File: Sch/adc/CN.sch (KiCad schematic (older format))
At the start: 19 parts, among them J1 JP4, J2 Header5, P1 CONN_02X40, U1 LTC2292

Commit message: Adding parts
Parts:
- C53: footprint (none) -> Capacitors_SMD:C_0603
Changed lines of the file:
@@
 F 0 "C53" H 3175 7050 50  0000 L CNN
 F 1 "0.1u" H 3175 6850 50  0000 L CNN
-F 2 "" H 3188 6800 50  0001 C CNN
+F 2 "Capacitors_SMD:C_0603" H 3188 6800 50  0001 C CNN
 F 3 "" H 3150 6950 50  0000 C CNN
 	1    3150 6950

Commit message: Add parts
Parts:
- J1: footprint (none) -> Pin_Headers:Pin_Header_Straight_2x04_Pitch2.54mm
- J2: footprint (none) -> Pin_Headers:Pin_Header_Straight_1x05_Pitch2.54mm
- R1, R12, R24, R25, R26: footprint (none) -> Resistors_SMD:R_0603
- R10, R11: value 49k -> 10k; footprint (none) -> Resistors_SMD:R_0603
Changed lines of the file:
@@
 F 0 "R24" V 1880 6150 50  0000 C CNN
 F 1 "1k" V 1800 6150 50  0000 C CNN
-F 2 "" V 1730 6150 50  0001 C CNN
+F 2 "Resistors_SMD:R_0603" V 1730 6150 50  0001 C CNN
 F 3 "" H 1800 6150 50  0000 C CNN
 	1    1800 6150
@@
 F 0 "R25" V 1880 6550 50  0000 C CNN
 F 1 "1k" V 1800 6550 50  0000 C CNN
-F 2 "" V 1730 6550 50  0001 C CNN
+F 2 "Resistors_SMD:R_0603" V 1730 6550 50  0001 C CNN
 F 3 "" H 1800 6550 50  0000 C CNN
 	1    1800 6550
@@
 F 0 "R26" V 1880 6950 50  0000 C CNN
 F 1 "1k" V 1800 6950 50  0000 C CNN
-F 2 "" V 1730 6950 50  0001 C CNN
+F 2 "Resistors_SMD:R_0603" V 1730 6950 50  0001 C CNN
 F 3 "" H 1800 6950 50  0000 C CNN
 	1    1800 6950
@@
 F 0 "J1" H 2600 6350 60  0000 C CNN
 F 1 "JP4" H 2600 7000 60  0000 C CNN
-F 2 "" H 2550 6900 60  0001 C CNN
+F 2 "Pin_Headers:Pin_Header_Straight_2x04_Pitch2.54mm" H 2550 6900 60  0001 C CNN
 F 3 "" H 2550 6900 60  0001 C CNN
 	1    2550 6650
@@
 F 0 "J2" H 8350 1850 60  0000 C CNN
 F 1 "Header5" H 8400 2500 60  0000 C CNN
-F 2 "" H 8350 2250 60  0001 C CNN
+F 2 "Pin_Headers:Pin_Header_Straight_1x05_Pitch2.54mm" H 8350 2250 60  0001 C CNN
 F 3 "" H 8350 2250 60  0001 C CNN
 	1    8350 2150
@@
 F 0 "R1" V 1030 2800 50  0000 C CNN
 F 1 "10k" V 950 2800 50  0000 C CNN
-F 2 "" V 880 2800 50  0001 C CNN
+F 2 "Resistors_SMD:R_0603" V 880 2800 50  0001 C CNN
 F 3 "" H 950 2800 50  0000 C CNN
 	1    950  2800
@@
 P 1600 3200
 F 0 "R10" V 1680 3200 50  0000 C CNN
-F 1 "49k" V 1600 3200 50  0000 C CNN
-F 2 "" V 1530 3200 50  0001 C CNN
+F 1 "10k" V 1600 3200 50  0000 C CNN
+F 2 "Resistors_SMD:R_0603" V 1530 3200 50  0001 C CNN
 F 3 "" H 1600 3200 50  0000 C CNN
 	1    1600 3200
@@
 P 1750 3200
 F 0 "R11" V 1830 3200 50  0000 C CNN
-F 1 "49k" V 1750 3200 50  0000 C CNN
-F 2 "" V 1680 3200 50  0001 C CNN
+F 1 "10k" V 1750 3200 50  0000 C CNN
+F 2 "Resistors_SMD:R_0603" V 1680 3200 50  0001 C CNN
 F 3 "" H 1750 3200 50  0000 C CNN
 	1    1750 3200
@@
 F 0 "R12" V 5880 4050 50  0000 C CNN
 F 1 "22" V 5800 4050 50  0000 C CNN
-F 2 "" V 5730 4050 50  0001 C CNN
+F 2 "Resistors_SMD:R_0603" V 5730 4050 50  0001 C CNN
 F 3 "" H 5800 4050 50  0000 C CNN
 	1    5800 4050

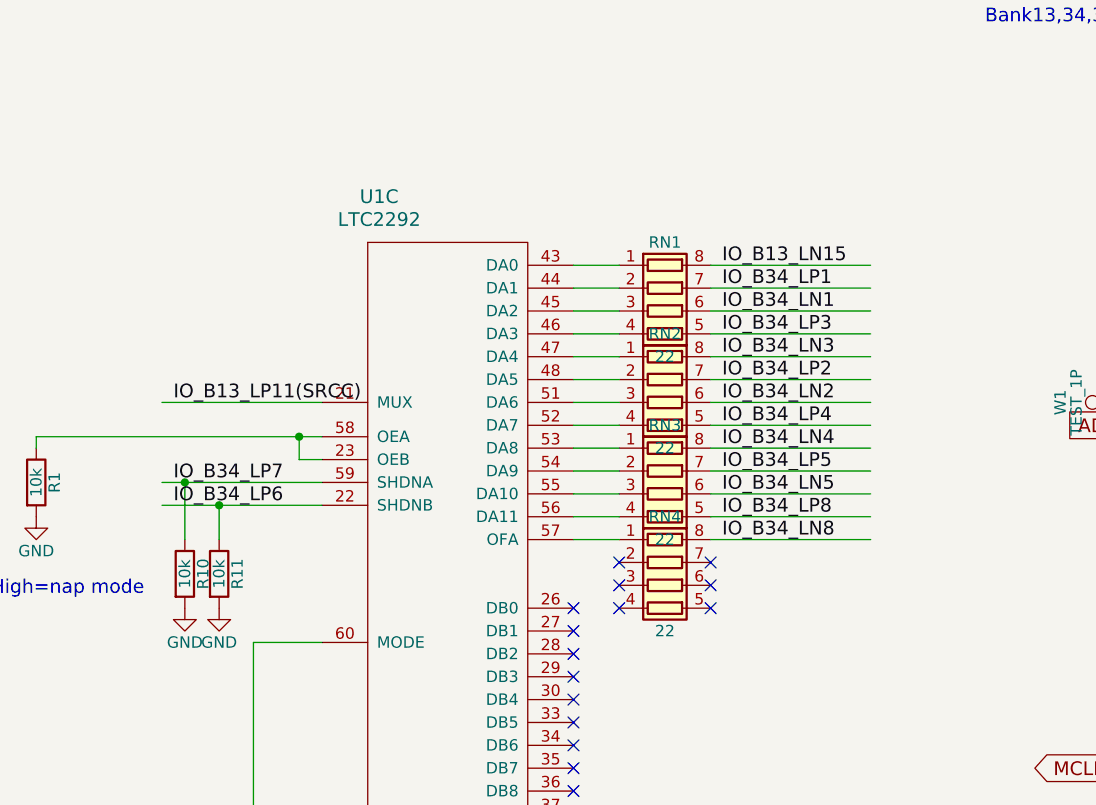
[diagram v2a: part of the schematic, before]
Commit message: Changed TCXO->MEMS TCXO. BOM finished
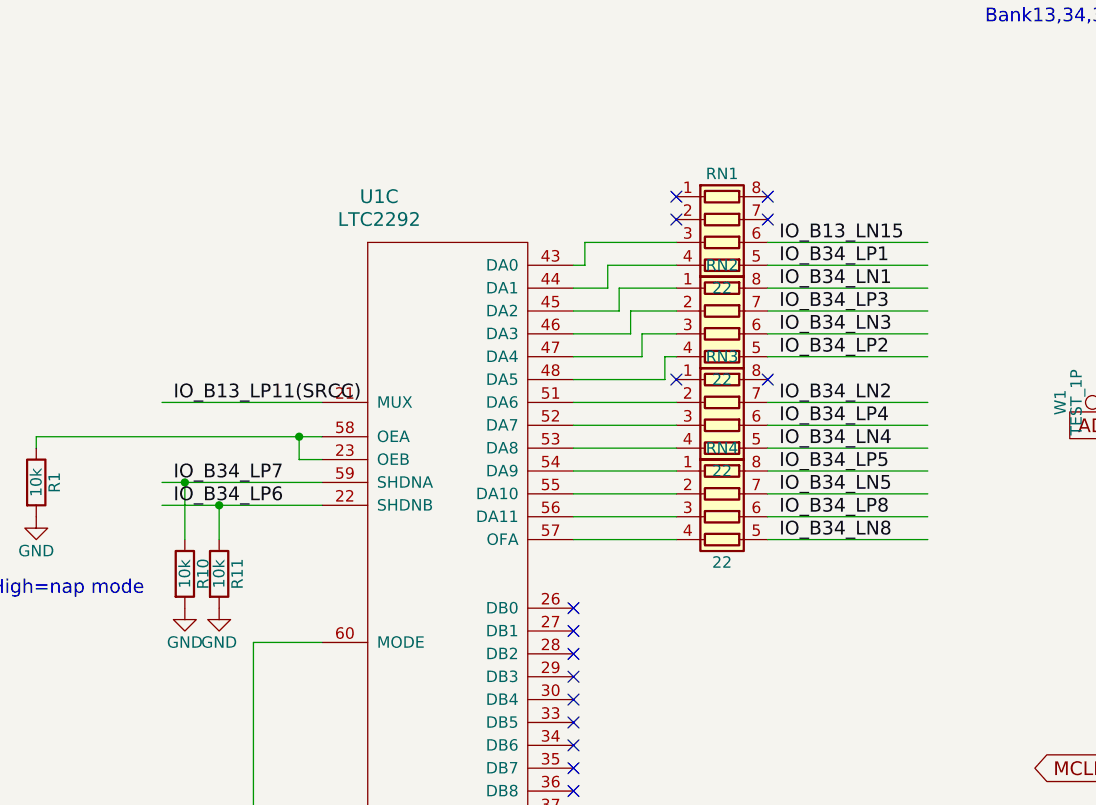
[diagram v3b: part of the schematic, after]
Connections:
- wire segments 114 -> 126
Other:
- moved on the sheet: RN1, RN2, RN3, RN4
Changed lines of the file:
@@
 Text Label 6000 2050 0    60   ~ 0
 IO_B13_LP11(SRCC)
-Text Label 3950 2750 0    60   ~ 0
+Text Label 4200 2750 0    60   ~ 0
 IO_B34_LP5
-Text Label 3950 2850 0    60   ~ 0
+Text Label 4200 2850 0    60   ~ 0
 IO_B34_LN5
-Text Label 3950 2950 0    60   ~ 0
+Text Label 4200 2950 0    60   ~ 0
 IO_B34_LP8
-Text Label 3950 3050 0    60   ~ 0
+Text Label 4200 3050 0    60   ~ 0
 IO_B34_LN8
-Text Label 3950 2650 0    60   ~ 0
+Text Label 4200 2650 0    60   ~ 0
 IO_B34_LN4
-Text Label 3950 2550 0    60   ~ 0
+Text Label 4200 2550 0    60   ~ 0
 IO_B34_LP4
-Text Label 3950 2450 0    60   ~ 0
+Text Label 4200 2450 0    60   ~ 0
 IO_B34_LN2
-Text Label 3950 2350 0    60   ~ 0
+Text Label 4200 2250 0    60   ~ 0
 IO_B34_LP2
-Text Label 3950 1950 0    60   ~ 0
+Text Label 4200 1850 0    60   ~ 0
 IO_B34_LP1
-Text Label 3950 2050 0    60   ~ 0
+Text Label 4200 1950 0    60   ~ 0
 IO_B34_LN1
-Text Label 3950 2150 0    60   ~ 0
+Text Label 4200 2050 0    60   ~ 0
 IO_B34_LP3
-Text Label 3950 2250 0    60   ~ 0
+Text Label 4200 2150 0    60   ~ 0
 IO_B34_LN3
-Text Label 3950 1850 0    60   ~ 0
+Text Label 4200 1750 0    60   ~ 0
 IO_B13_LN15
 Text Label 1550 2800 0    60   ~ 0
@@
 L R_Pack04 RN1
 U 1 1 58A5BF52
-P 3700 2050
-F 0 "RN1" V 3400 2050 50  0000 C CNN
-F 1 "22" V 3900 2050 50  0000 C CNN
-F 2 "" V 3975 2050 50  0001 C CNN
-F 3 "" H 3700 2050 50  0000 C CNN
-	1    3700 2050
+P 3950 1750
+F 0 "RN1" V 3650 1750 50  0000 C CNN
+F 1 "22" V 4150 1750 50  0000 C CNN
+F 2 "" V 4225 1750 50  0001 C CNN
+F 3 "" H 3950 1750 50  0000 C CNN
+	1    3950 1750
 	0    1    1    0
 $EndComp
@@
 L R_Pack04 RN2
 U 1 1 58A5BFD7
-P 3700 2450
-F 0 "RN2" V 3400 2450 50  0000 C CNN
-F 1 "22" V 3900 2450 50  0000 C CNN
-F 2 "" V 3975 2450 50  0001 C CNN
-F 3 "" H 3700 2450 50  0000 C CNN
-	1    3700 2450
+P 3950 2150
+F 0 "RN2" V 3650 2150 50  0000 C CNN
+F 1 "22" V 4150 2150 50  0000 C CNN
+F 2 "" V 4225 2150 50  0001 C CNN
+F 3 "" H 3950 2150 50  0000 C CNN
+	1    3950 2150
 	0    1    1    0
 $EndComp
@@
 L R_Pack04 RN3
 U 1 1 58A5C027
-P 3700 2850
-F 0 "RN3" V 3400 2850 50  0000 C CNN
-F 1 "22" V 3900 2850 50  0000 C CNN
-F 2 "" V 3975 2850 50  0001 C CNN
-F 3 "" H 3700 2850 50  0000 C CNN
-	1    3700 2850
+P 3950 2550
+F 0 "RN3" V 3650 2550 50  0000 C CNN
+F 1 "22" V 4150 2550 50  0000 C CNN
+F 2 "" V 4225 2550 50  0001 C CNN
+F 3 "" H 3950 2550 50  0000 C CNN
+	1    3950 2550
 	0    1    1    0
 $EndComp
@@
 L R_Pack04 RN4
 U 1 1 58A5C02D
-P 3700 3250
-F 0 "RN4" V 3400 3250 50  0000 C CNN
-F 1 "22" V 3900 3250 50  0000 C CNN
-F 2 "" V 3975 3250 50  0001 C CNN
-F 3 "" H 3700 3250 50  0000 C CNN
-	1    3700 3250
+P 3950 2950
+F 0 "RN4" V 3650 2950 50  0000 C CNN
+F 1 "22" V 4150 2950 50  0000 C CNN
+F 2 "" V 4225 2950 50  0001 C CNN
+F 3 "" H 3950 2950 50  0000 C CNN
+	1    3950 2950
 	0    1    1    0
 $EndComp
-NoConn ~ 3500 3150
-NoConn ~ 3500 3250
-NoConn ~ 3500 3350
-NoConn ~ 3900 3350
-NoConn ~ 3900 3250
-NoConn ~ 3900 3150
+NoConn ~ 3750 1550
+NoConn ~ 3750 1650
 Text Notes 7950 3800 0    60   ~ 0
 LED
@@
 	7150 3750 7850 3750
 Wire Wire Line
-	3900 2750 4600 2750
-Wire Wire Line
-	3900 2850 4600 2850
-Wire Wire Line
-	3900 2950 4600 2950
-Wire Wire Line
-	3900 3050 4600 3050
-Wire Wire Line
-	4600 2350 3900 2350
-Wire Wire Line
-	4600 2450 3900 2450
-Wire Wire Line
-	4600 2550 3900 2550
-Wire Wire Line
-	4600 2650 3900 2650
-Wire Wire Line
-	3900 1950 4600 1950
-Wire Wire Line
-	3900 2050 4600 2050
-Wire Wire Line
-	3900 2150 4600 2150
-Wire Wire Line
-	3900 2250 4600 2250
-Wire Wire Line
-	4600 1850 3900 1850
+	4150 2750 4850 2750
+Wire Wire Line
+	4150 2850 4850 2850
+Wire Wire Line
+	4150 2950 4850 2950
+Wire Wire Line
+	4150 3050 4850 3050
+Wire Wire Line
+	4850 2250 4150 2250
+Wire Wire Line
+	4850 2450 4150 2450
+Wire Wire Line
+	4850 2550 4150 2550
+Wire Wire Line
+	4850 2650 4150 2650
+Wire Wire Line
+	4150 1850 4850 1850
+Wire Wire Line
+	4150 1950 4850 1950
+Wire Wire Line
+	4150 2050 4850 2050
+Wire Wire Line
+	4150 2150 4850 2150
+Wire Wire Line
+	4850 1750 4150 1750
 Wire Wire Line
 	950  2600 2200 2600
 Wire Wire Line
-	2200 2800 1500 2800
+	1500 2800 2200 2800
 Wire Wire Line
 	2200 2450 1500 2450
@@
 	7150 2250 8150 2250
 Wire Wire Line
-	3300 1850 3500 1850
-Wire Wire Line
-	3300 1950 3500 1950
-Wire Wire Line
-	3300 2050 3500 2050
-Wire Wire Line
-	3300 2150 3500 2150
-Wire Wire Line
-	3300 2250 3500 2250
-Wire Wire Line
-	3300 2350 3500 2350
-Wire Wire Line
-	3300 2450 3500 2450
-Wire Wire Line
-	3300 2550 3500 2550
-Wire Wire Line
-	3300 2650 3500 2650
-Wire Wire Line
-	3300 2750 3500 2750
-Wire Wire Line
-	3300 2850 3500 2850
-Wire Wire Line
-	3300 2950 3500 2950
-Wire Wire Line
-	3300 3050 3500 3050
+	3300 2450 3750 2450
+Wire Wire Line
+	3300 2550 3750 2550
+Wire Wire Line
+	3300 2650 3750 2650
+Wire Wire Line
+	3300 2750 3750 2750
+Wire Wire Line
+	3300 2850 3750 2850
+Wire Wire Line
+	3300 2950 3750 2950
+Wire Wire Line
+	3300 3050 3750 3050
 Wire Wire Line
 	1500 2900 2200 2900
@@
 	1    0    0    -1
 $EndComp
+Wire Wire Line
+	3300 2350 3700 2350
+Wire Wire Line
+	3700 2350 3700 2250
+Wire Wire Line
+	3700 2250 3750 2250
+Wire Wire Line
+	3300 2250 3600 2250
+Wire Wire Line
+	3600 2250 3600 2150
+Wire Wire Line
+	3600 2150 3750 2150
+NoConn ~ 3750 2350
+Wire Wire Line
+	3300 2150 3550 2150
+Wire Wire Line
+	3550 2150 3550 2050
+Wire Wire Line
+	3550 2050 3750 2050
+Wire Wire Line
+	3300 2050 3500 2050
+Wire Wire Line
+	3500 2050 3500 1950
+Wire Wire Line
+	3500 1950 3750 1950
+Wire Wire Line
+	3300 1950 3450 1950
+Wire Wire Line
+	3450 1950 3450 1850
+Wire Wire Line
+	3450 1850 3750 1850
+Wire Wire Line
+	3300 1850 3350 1850
+Wire Wire Line
+	3350 1850 3350 1750
+Wire Wire Line
+	3350 1750 3750 1750
+NoConn ~ 4150 2350
+NoConn ~ 4150 1550
+NoConn ~ 4150 1650
 $EndSCHEMATC

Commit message: Assigned footprint to all the parts
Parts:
- C53: footprint Capacitors_SMD:C_0603 -> adc_lib:C0603
- J1: footprint Pin_Headers:Pin_Header_Straight_2x04_Pitch2.54mm -> adc_lib:M20-9980445
- J2: footprint Pin_Headers:Pin_Header_Straight_1x05_Pitch2.54mm -> adc_lib:M20-9990546
- P1: footprint (none) -> adc_lib:20021121-00080T4LF
- R1, R10, R11, R12, R24, R25, R26: footprint Resistors_SMD:R_0603 -> adc_lib:R0603
- RN1, RN2, RN3, RN4, RN5: footprint (none) -> adc_lib:EXB-38V220JV
- U1: footprint (none) -> adc_lib:LTC2292
- W1, W2: footprint (none) -> adc_lib:68000-401HLF
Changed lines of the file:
@@
 F 0 "U1" H 2450 4850 60  0000 C CNN
 F 1 "LTC2292" H 2450 4750 60  0000 C CNN
-F 2 "" H 2750 3200 60  0001 C CNN
+F 2 "adc_lib:LTC2292" H 2750 3200 60  0001 C CNN
 F 3 "" H 2750 3200 60  0001 C CNN
 	3    2750 3200
@@
 F 0 "P1" H 6900 5750 50  0000 C CNN
 F 1 "CONN_02X40" V 6900 3700 50  0000 C CNN
-F 2 "" H 6900 3700 50  0001 C CNN
+F 2 "adc_lib:20021121-00080T4LF" H 6900 3700 50  0001 C CNN
 F 3 "" H 6900 3700 50  0000 C CNN
 	1    6900 3700
@@
 F 0 "R24" V 1880 6150 50  0000 C CNN
 F 1 "1k" V 1800 6150 50  0000 C CNN
-F 2 "Resistors_SMD:R_0603" V 1730 6150 50  0001 C CNN
+F 2 "adc_lib:R0603" V 1730 6150 50  0001 C CNN
 F 3 "" H 1800 6150 50  0000 C CNN
 	1    1800 6150
@@
 F 0 "R25" V 1880 6550 50  0000 C CNN
 F 1 "1k" V 1800 6550 50  0000 C CNN
-F 2 "Resistors_SMD:R_0603" V 1730 6550 50  0001 C CNN
+F 2 "adc_lib:R0603" V 1730 6550 50  0001 C CNN
 F 3 "" H 1800 6550 50  0000 C CNN
 	1    1800 6550
@@
 F 0 "R26" V 1880 6950 50  0000 C CNN
 F 1 "1k" V 1800 6950 50  0000 C CNN
-F 2 "Resistors_SMD:R_0603" V 1730 6950 50  0001 C CNN
+F 2 "adc_lib:R0603" V 1730 6950 50  0001 C CNN
 F 3 "" H 1800 6950 50  0000 C CNN
 	1    1800 6950
@@
 F 0 "C53" H 3175 7050 50  0000 L CNN
 F 1 "0.1u" H 3175 6850 50  0000 L CNN
-F 2 "Capacitors_SMD:C_0603" H 3188 6800 50  0001 C CNN
+F 2 "adc_lib:C0603" H 3188 6800 50  0001 C CNN
 F 3 "" H 3150 6950 50  0000 C CNN
 	1    3150 6950
@@
 F 0 "J1" H 2600 6350 60  0000 C CNN
 F 1 "JP4" H 2600 7000 60  0000 C CNN
-F 2 "Pin_Headers:Pin_Header_Straight_2x04_Pitch2.54mm" H 2550 6900 60  0001 C CNN
+F 2 "adc_lib:M20-9980445" H 2550 6900 60  0001 C CNN
 F 3 "" H 2550 6900 60  0001 C CNN
 	1    2550 6650
@@
 F 0 "J2" H 8350 1850 60  0000 C CNN
 F 1 "Header5" H 8400 2500 60  0000 C CNN
-F 2 "Pin_Headers:Pin_Header_Straight_1x05_Pitch2.54mm" H 8350 2250 60  0001 C CNN
+F 2 "adc_lib:M20-9990546" H 8350 2250 60  0001 C CNN
 F 3 "" H 8350 2250 60  0001 C CNN
 	1    8350 2150
@@
 F 0 "RN1" V 3650 1750 50  0000 C CNN
 F 1 "22" V 4150 1750 50  0000 C CNN
-F 2 "" V 4225 1750 50  0001 C CNN
+F 2 "adc_lib:EXB-38V220JV" V 4225 1750 50  0001 C CNN
 F 3 "" H 3950 1750 50  0000 C CNN
 	1    3950 1750
@@
 F 0 "RN2" V 3650 2150 50  0000 C CNN
 F 1 "22" V 4150 2150 50  0000 C CNN
-F 2 "" V 4225 2150 50  0001 C CNN
+F 2 "adc_lib:EXB-38V220JV" V 4225 2150 50  0001 C CNN
 F 3 "" H 3950 2150 50  0000 C CNN
 	1    3950 2150
@@
 F 0 "RN3" V 3650 2550 50  0000 C CNN
 F 1 "22" V 4150 2550 50  0000 C CNN
-F 2 "" V 4225 2550 50  0001 C CNN
+F 2 "adc_lib:EXB-38V220JV" V 4225 2550 50  0001 C CNN
 F 3 "" H 3950 2550 50  0000 C CNN
 	1    3950 2550
@@
 F 0 "RN4" V 3650 2950 50  0000 C CNN
 F 1 "22" V 4150 2950 50  0000 C CNN
-F 2 "" V 4225 2950 50  0001 C CNN
+F 2 "adc_lib:EXB-38V220JV" V 4225 2950 50  0001 C CNN
 F 3 "" H 3950 2950 50  0000 C CNN
 	1    3950 2950
@@
 F 0 "R1" V 1030 2800 50  0000 C CNN
 F 1 "10k" V 950 2800 50  0000 C CNN
-F 2 "Resistors_SMD:R_0603" V 880 2800 50  0001 C CNN
+F 2 "adc_lib:R0603" V 880 2800 50  0001 C CNN
 F 3 "" H 950 2800 50  0000 C CNN
 	1    950  2800
@@
 F 0 "R10" V 1680 3200 50  0000 C CNN
 F 1 "10k" V 1600 3200 50  0000 C CNN
-F 2 "Resistors_SMD:R_0603" V 1530 3200 50  0001 C CNN
+F 2 "adc_lib:R0603" V 1530 3200 50  0001 C CNN
 F 3 "" H 1600 3200 50  0000 C CNN
 	1    1600 3200
@@
 F 0 "R11" V 1830 3200 50  0000 C CNN
 F 1 "10k" V 1750 3200 50  0000 C CNN
-F 2 "Resistors_SMD:R_0603" V 1680 3200 50  0001 C CNN
+F 2 "adc_lib:R0603" V 1680 3200 50  0001 C CNN
 F 3 "" H 1750 3200 50  0000 C CNN
 	1    1750 3200
@@
 F 0 "RN5" V 8550 2650 50  0000 C CNN
 F 1 "22" V 9050 2650 50  0000 C CNN
-F 2 "" V 9125 2650 50  0001 C CNN
+F 2 "adc_lib:EXB-38V220JV" V 9125 2650 50  0001 C CNN
 F 3 "" H 8850 2650 50  0000 C CNN
 	1    8850 2650
@@
 F 0 "R12" V 5880 4050 50  0000 C CNN
 F 1 "22" V 5800 4050 50  0000 C CNN
-F 2 "Resistors_SMD:R_0603" V 5730 4050 50  0001 C CNN
+F 2 "adc_lib:R0603" V 5730 4050 50  0001 C CNN
 F 3 "" H 5800 4050 50  0000 C CNN
 	1    5800 4050
@@
 F 0 "W1" H 5700 2720 50  0000 C CNN
 F 1 "TEST_1P" H 5700 2650 50  0000 C CNN
-F 2 "" H 5900 2450 50  0001 C CNN
+F 2 "adc_lib:68000-401HLF" H 5900 2450 50  0001 C CNN
 F 3 "" H 5900 2450 50  0000 C CNN
 	1    5700 2450
@@
 F 0 "W2" H 9850 1470 50  0000 C CNN
 F 1 "TEST_1P" H 9850 1400 50  0000 C CNN
-F 2 "" H 10050 1200 50  0001 C CNN
+F 2 "adc_lib:68000-401HLF" H 10050 1200 50  0001 C CNN
 F 3 "" H 10050 1200 50  0000 C CNN
 	1    9850 1200

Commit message: layout more
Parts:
- added R3: 10k, adc_lib:R0603, symbol R
- C53: footprint adc_lib:C0603 -> adc_lib:C0402
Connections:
- wire segments 126 -> 125
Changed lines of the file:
@@
 F 0 "C53" H 3175 7050 50  0000 L CNN
 F 1 "0.1u" H 3175 6850 50  0000 L CNN
-F 2 "adc_lib:C0603" H 3188 6800 50  0001 C CNN
+F 2 "adc_lib:C0402" H 3188 6800 50  0001 C CNN
 F 3 "" H 3150 6950 50  0000 C CNN
 	1    3150 6950
@@
 	1500 2900 2200 2900
 Wire Wire Line
-	2100 2600 2100 2700
-Wire Wire Line
-	2100 2700 2200 2700
-Connection ~ 2100 2600
+	1150 2700 2200 2700
 Wire Wire Line
 	1550 5700 1800 5700
@@
 NoConn ~ 4150 1550
 NoConn ~ 4150 1650
+$Comp
+L R R3
+U 1 1 58B07F2F
+P 1150 2850
+F 0 "R3" V 1230 2850 50  0000 C CNN
+F 1 "10k" V 1150 2850 50  0000 C CNN
+F 2 "adc_lib:R0603" V 1080 2850 50  0001 C CNN
+F 3 "" H 1150 2850 50  0000 C CNN
+	1    1150 2850
+	1    0    0    -1
+$EndComp
+$Comp
+L GND #PWR014
+U 1 1 58B07F94
+P 1150 3000
+F 0 "#PWR014" H 1150 2750 50  0001 C CNN
+F 1 "GND" H 1150 2850 50  0000 C CNN
+F 2 "" H 1150 3000 50  0000 C CNN
+F 3 "" H 1150 3000 50  0000 C CNN
+	1    1150 3000
+	1    0    0    -1
+$EndComp
 $EndSCHEMATC
